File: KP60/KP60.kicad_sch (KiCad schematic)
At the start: 18 parts, among them J1 USB_C_Receptacle_USB2.0_14P, SW2 SW_Push, U1 USBLC6-2SC6, U2 STM32F072CBTx, U3 XC6206PxxxMR

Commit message: more images + naming fixes
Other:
- title: KP1800 Keyboard PCB -> KP60 Keyboard PCB
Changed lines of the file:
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@@
 	(paper "A4")
 	(title_block
-		(title "KP1800 Keyboard PCB")
-		(date "2025-05-02")
+		(title "KP60 Keyboard PCB")
+		(date "2025-05-03")
 		(rev "0.1")
 	)

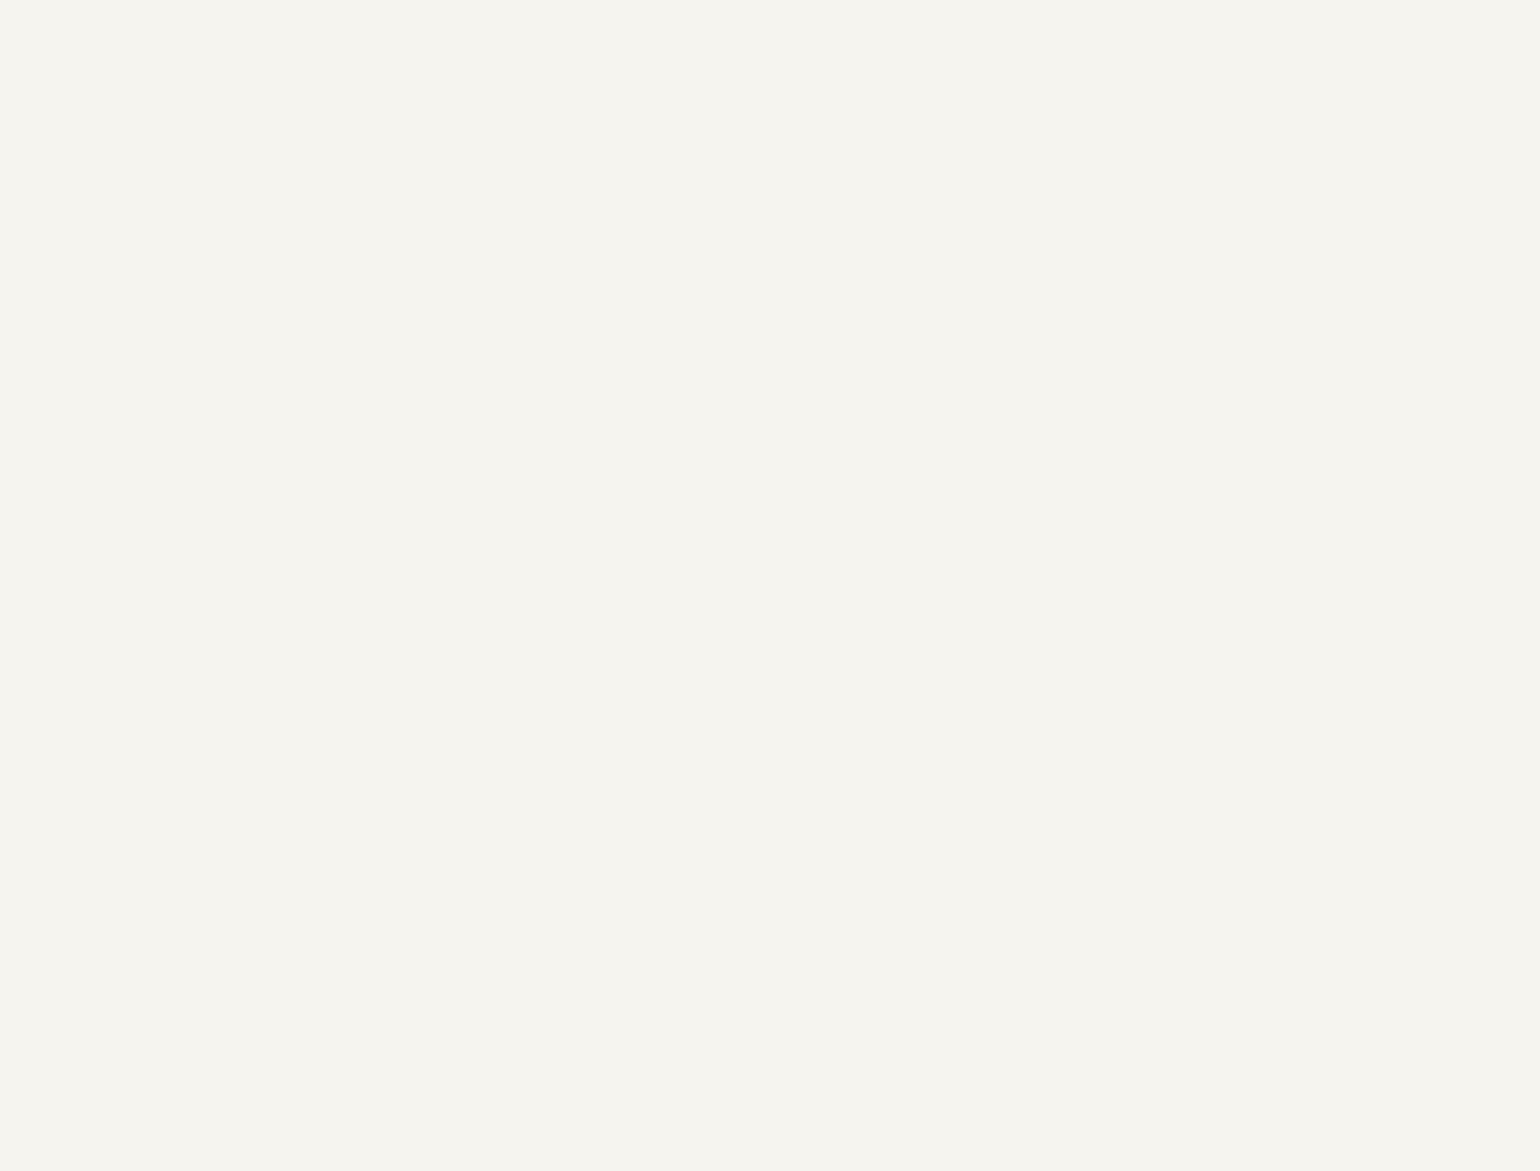
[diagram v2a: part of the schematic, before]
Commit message: add led matrix circuit + passed ERC
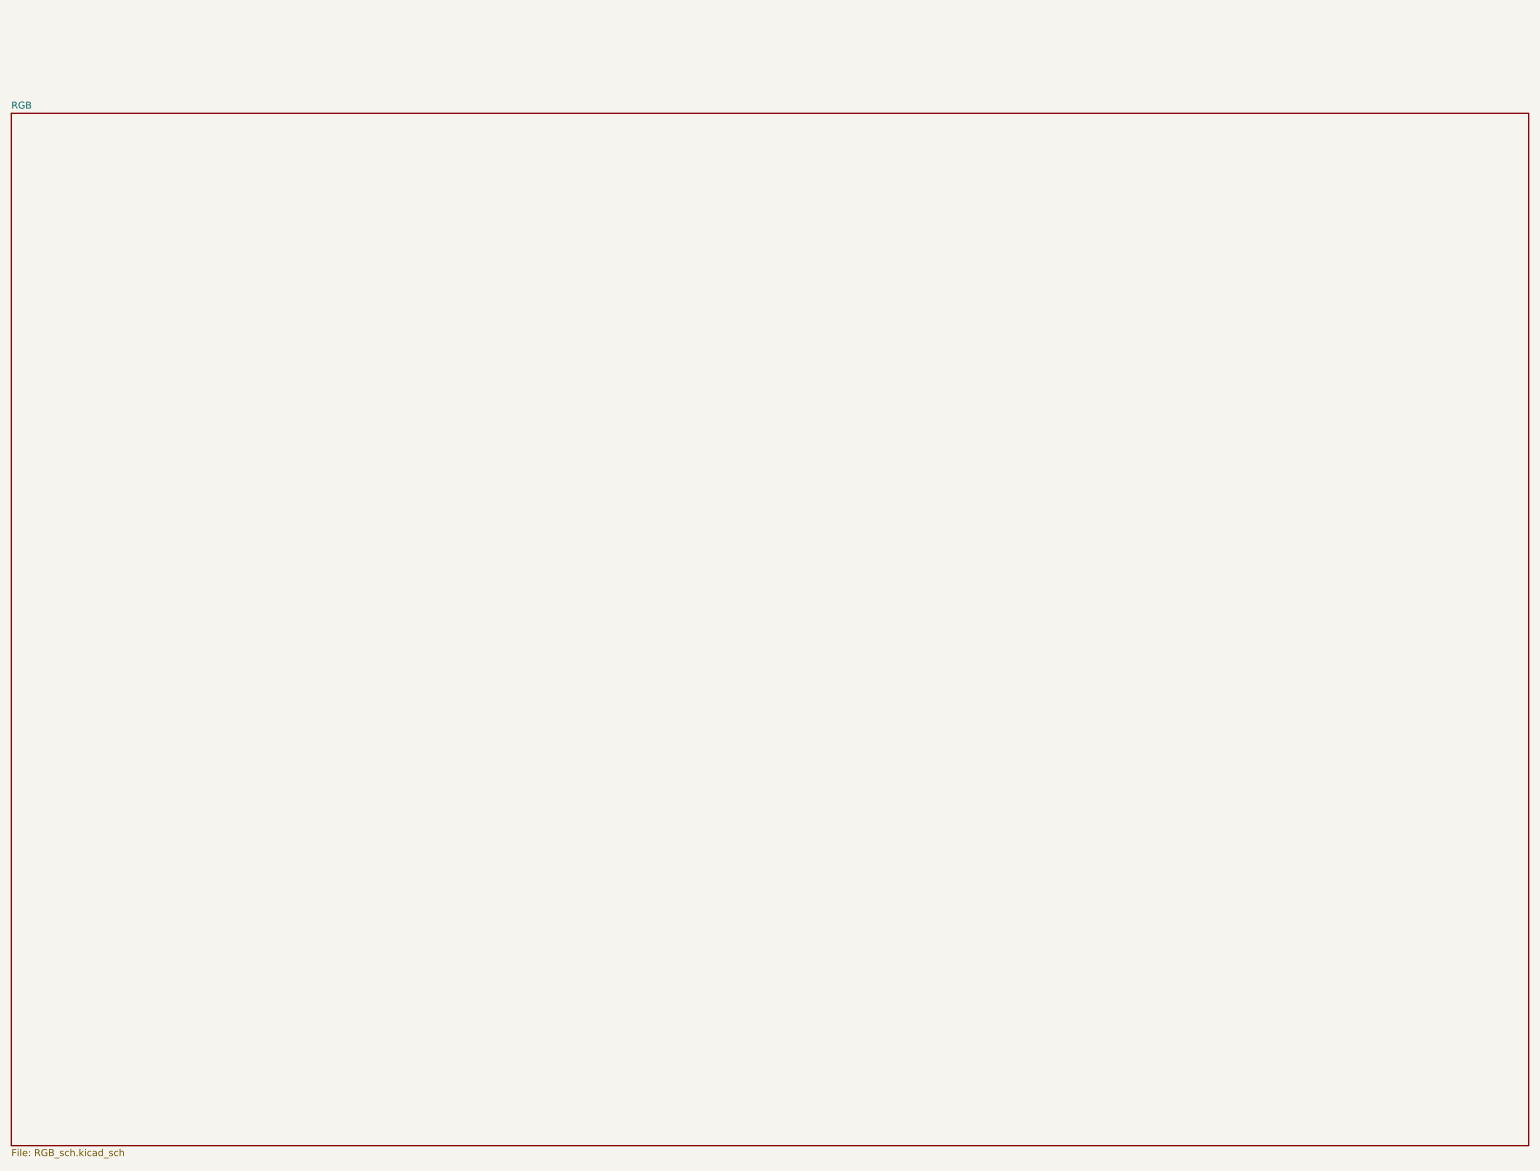
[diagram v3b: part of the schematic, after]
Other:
- added sheet RGB (RGB_sch.kicad_sch)
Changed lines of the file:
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@@
+		)
+	)
+	(sheet
+		(at 10.16 441.96)
+		(size 278.13 189.23)
+		(fields_autoplaced yes)
+		(stroke
+			(width 0.1524)
+			(type solid)
+		)
+		(fill
+			(color 0 0 0 0.0000)
+		)
+		(property "Sheetname" "RGB"
+			(at 10.16 441.2484 0)
+			(effects
+				(font
+					(size 1.27 1.27)
+				)
+				(justify left bottom)
+			)
+		)
+		(property "Sheetfile" "RGB_sch.kicad_sch"
+			(at 10.16 631.7746 0)
+			(effects
+				(font
+					(size 1.27 1.27)
+				)
+				(justify left top)
+			)
+		)
+		(instances
+			(project "KP60"
+				(path "/7108c105-5751-4eb7-aac4-6c879069d1a1"
+					(page "3")
+				)
+			)
 		)
 	)

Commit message: Formatting Changes
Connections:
- net A2: now reaches U2.12 (PA2)
- no-connect marks 16 -> 15
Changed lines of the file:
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@@
-	)
-	(no_connect
-		(at 116.84 64.77)
 	)
 	(no_connect
@@
 			(effects
 				(font
+					(size 1.27 1.27)
+				)
+				(justify left)
+				(hide yes)
+			)
+		)
+	)
+	(global_label "A2"
+		(shape input)
+		(at 116.84 64.77 0)
+		(fields_autoplaced yes)
+		(effects
+			(font
+				(size 1.27 1.27)
+			)
+			(justify left)
+		)
+		(property "Intersheetrefs" "${INTERSHEET_REFS}"
+			(at 122.1233 64.77 0)
+			(effects
+				(font

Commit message: diff. trace tweaks
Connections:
- net CC1: now reaches J1.A5 (CC1), R3.2
- net CC2: now reaches J1.B5 (CC2), R2.2
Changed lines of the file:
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@@
+		)
+	)
+	(label "CC2"
+		(at 204.47 69.85 0)
+		(fields_autoplaced yes)
+		(effects
+			(font
+				(size 1.27 1.27)
+			)
+			(justify left bottom)
 		)
 	)
@@
 			)
 			(justify left bottom)
+		)
+	)
+	(label "CC1"
+		(at 204.47 67.31 0)
+		(fields_autoplaced yes)
+		(effects
+			(font
+				(size 1.27 1.27)
+			)
+			(justify left bottom)
